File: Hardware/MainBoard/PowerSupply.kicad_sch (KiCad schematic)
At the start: 7 parts, among them J5 USB_B_Micro, U3 LD1117ASTR

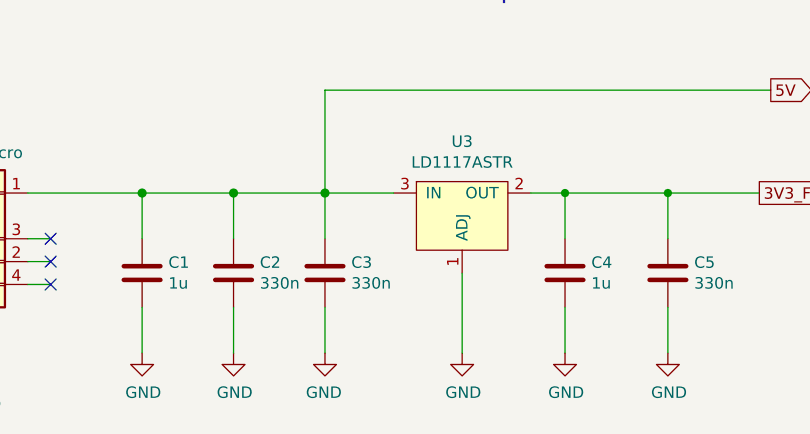
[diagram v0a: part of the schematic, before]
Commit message: make boards smaller, fix sd card slot
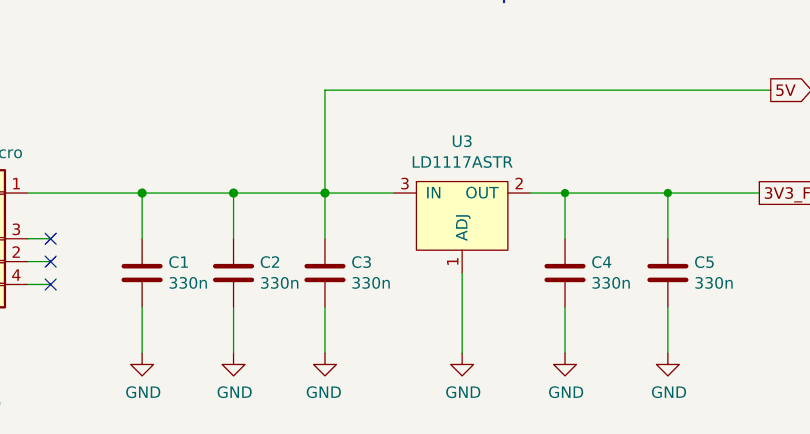
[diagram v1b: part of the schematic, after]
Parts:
- C1, C4: value 1u -> 330n
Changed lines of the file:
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@@
 			)
 		)
-		(property "Value" "1u"
+		(property "Value" "330n"
 			(at 117.221 93.853 0)
 			(effects
@@
 			)
 		)
-		(property "Value" "1u"
+		(property "Value" "330n"
 			(at 70.231 93.853 0)
 			(effects

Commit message: xx
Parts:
- removed U3: LD1117ASTR, Package_TO_SOT_SMD:SOT-223, symbol MainBoard:LD1117ASTR
- added D4: LED, LED_SMD:LED_0402_1005Metric, symbol Device:LED
- added JP1: Jumper_2_Open, Connector_PinHeader_2.54mm:PinHeader_1x02_P2.54mm_Vertical, symbol Jumper:Jumper_2_Open
- added R11: 1k, Resistor_SMD:R_0805_2012Metric, symbol Device:R
- added U1: LD1117S50TR_SOT223, Package_TO_SOT_SMD:SOT-223-3_TabPin2, symbol Regulator_Linear:LD1117S50TR_SOT223
- J5: footprint Connector_USB:USB_Micro-B_Molex-105017-0001 -> HardwareDataLogger:USB_Micro-B_Molex-105017-0001_Extra_Mechanical_Pads
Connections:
- net 3V3_FROM_MAINBOARD: now also U1.2 (VO)
- net 5V: now also JP1.1 (A), U1.3 (VI)
- net GND: now also D4.1 (K), U1.1 (GND)
- new net: JP1.2 (B), R11.1
- new net: D4.2 (A), R11.2
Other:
- note added: "NOTE: ESP acceptable supply voltage: 3v-3v6 STM32 has its own regulator: 5v input ST7735S acceptable supply voltage: 3v3 The device will be powered via USB (used only as a power supply, no USB communication) The ESP and ST7735S will be powered at 3v3 U1 is a fixed 3v3 voltage variant"
- note removed: "NOTE: ESP acceptable supply voltage: 3v-3v6 STM32 has its own regulator: 5v ST7735S acceptable supply voltage: 3v3 The device will be powered via USB (used only as a power supply, no USB communication) The ESP and ST7735S will be powered at 3v3 U3 is a fixed 3v3 voltage variant"
